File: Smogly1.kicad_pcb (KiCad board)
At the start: 2 copper layers, 92.2 x 68 mm, 9 parts, among them J1 VCC IN, J10 ESP32-DevKit VIN-EN, J11 ESP32-DevKit 3V3-D23, J2 PMSx003, J3 BME280, J4 microUSB, J5 5/3.3/GND, J8 D33/32/35/35, J9 PMS7003_Conn

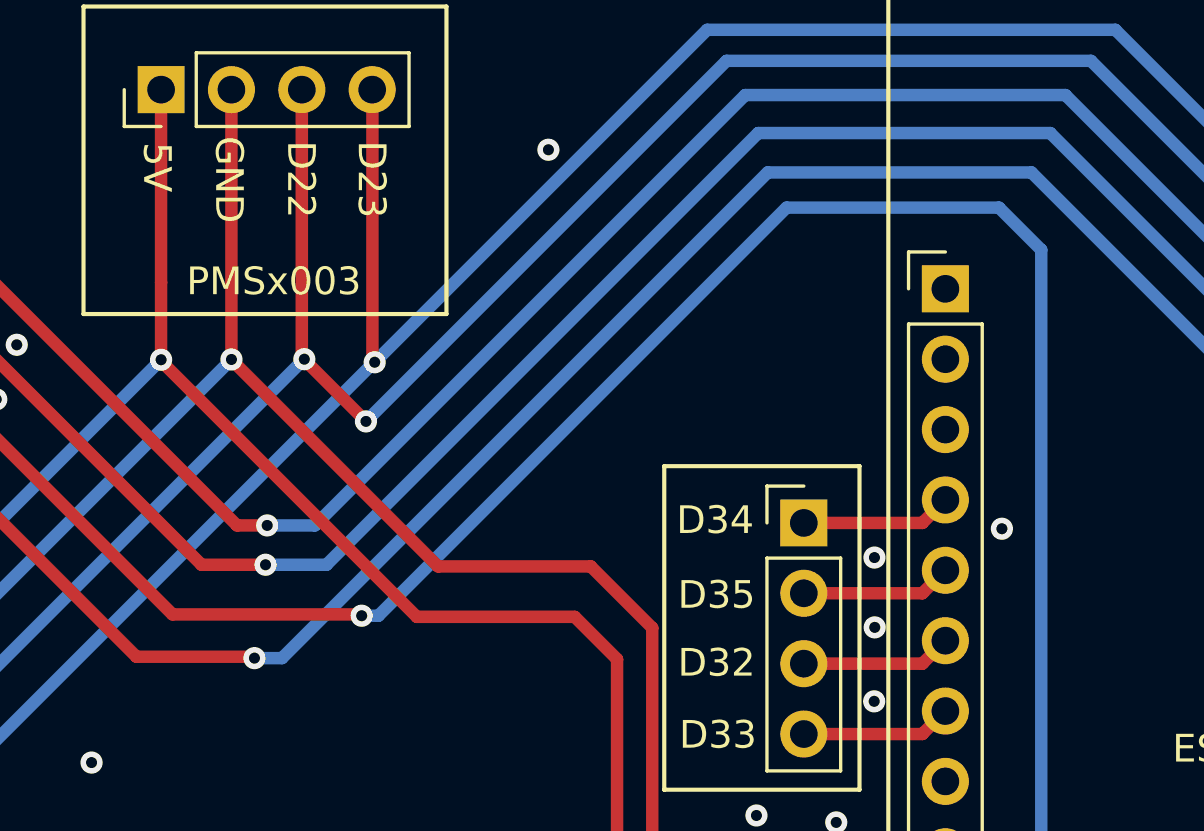
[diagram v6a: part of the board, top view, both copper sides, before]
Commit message: fixed wrong BME280 power connection (switch +3/G pins)
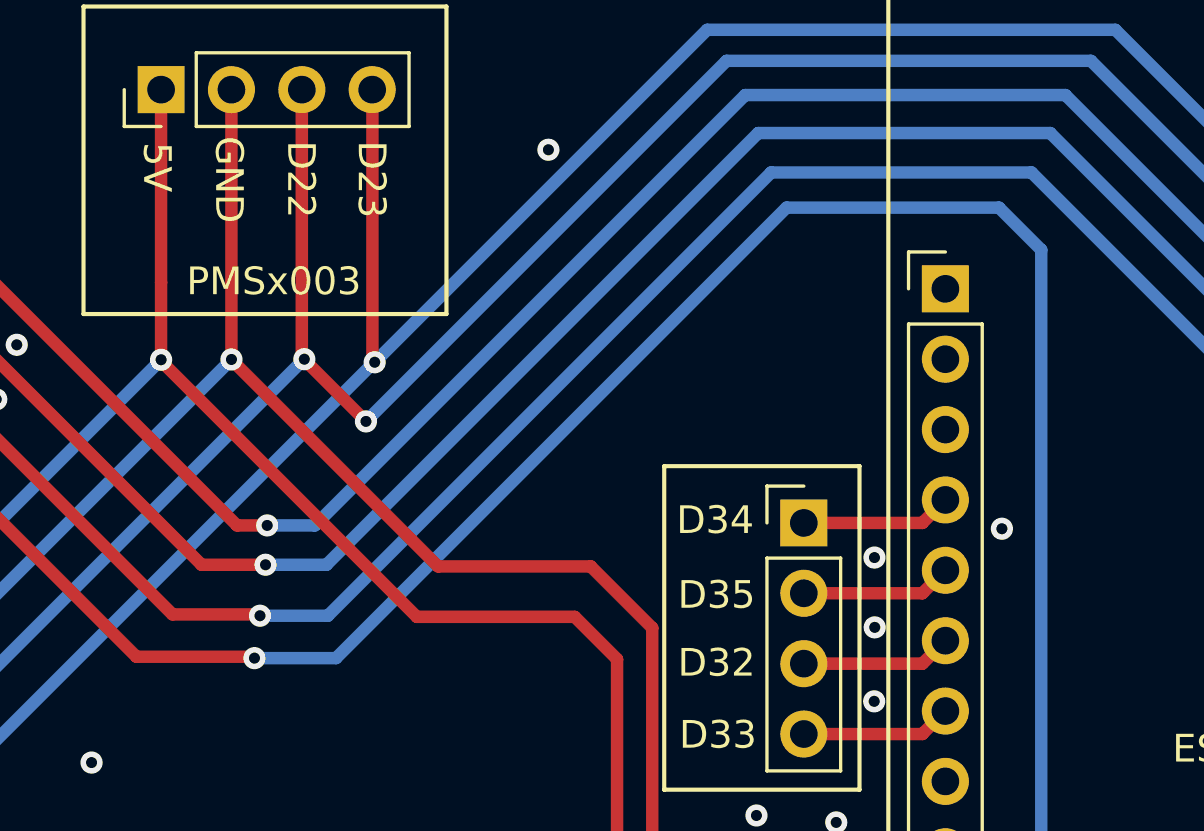
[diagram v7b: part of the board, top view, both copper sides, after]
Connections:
- J3 pad 3: +3V3 -> Net-(J11-Pad14)
- J3 pad 4: Net-(J11-Pad14) -> +3V3
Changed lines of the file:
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@@
       (net 13 "Net-(J11-Pad7)") (pinfunction "Pin_2") (pintype "passive"))
     (pad "3" thru_hole oval locked (at 0 5.08) (size 1.7 1.7) (drill 1) (layers *.Cu *.Mask)
-      (net 5 "+3V3") (pinfunction "Pin_3") (pintype "passive"))
+      (net 2 "Net-(J11-Pad14)") (pinfunction "Pin_3") (pintype "passive"))
     (pad "4" thru_hole oval locked (at 0 7.62) (size 1.7 1.7) (drill 1) (layers *.Cu *.Mask)
-      (net 2 "Net-(J11-Pad14)") (pinfunction "Pin_4") (pintype "passive"))
+      (net 5 "+3V3") (pinfunction "Pin_4") (pintype "passive"))
     (model "${KISYS3DMOD}/Connector_PinHeader_2.54mm.3dshapes/PinHeader_1x04_P2.54mm_Vertical.wrl"
       (offset (xyz 0 0 0))
@@
   (segment (start 250.39 82.65) (end 250.5 82.54) (width 0.45) (layer "B.Cu") (net 1))
   (segment (start 177.68 109.85) (end 177.68 107.02) (width 0.45) (layer "B.Cu") (net 1))
-  (segment (start 188.15 85.32) (end 185 85.32) (width 0.45) (layer "F.Cu") (net 2))
-  (segment (start 200.37 93.33) (end 200.32 93.28) (width 0.45) (layer "F.Cu") (net 2))
-  (segment (start 200.32 93.28) (end 196.11 93.28) (width 0.45) (layer "F.Cu") (net 2))
-  (segment (start 196.11 93.28) (end 188.15 85.32) (width 0.45) (layer "F.Cu") (net 2))
-  (via (at 200.37 93.33) (size 0.8) (drill 0.4) (layers "F.Cu" "B.Cu") (net 2))
-  (segment (start 218.8958 75.7992) (end 228.4192 75.7992) (width 0.45) (layer "B.Cu") (net 2))
+  (segment (start 188.44 82.78) (end 185 82.78) (width 0.45) (layer "F.Cu") (net 2))
+  (segment (start 197.41 91.75) (end 188.44 82.78) (width 0.45) (layer "F.Cu") (net 2))
+  (segment (start 200.52 91.75) (end 197.41 91.75) (width 0.45) (layer "F.Cu") (net 2))
+  (segment (start 200.57 91.8) (end 200.52 91.75) (width 0.45) (layer "F.Cu") (net 2))
+  (via (at 200.57 91.8) (size 0.8) (drill 0.4) (layers "F.Cu" "B.Cu") (net 2))
   (segment (start 246.37 108.89) (end 250.5 113.02) (width 0.45) (layer "B.Cu") (net 2))
-  (segment (start 201.365 93.33) (end 218.8958 75.7992) (width 0.45) (layer "B.Cu") (net 2))
+  (segment (start 203.02 91.8) (end 219.0208 75.7992) (width 0.45) (layer "B.Cu") (net 2))
+  (segment (start 246.37 93.75) (end 246.37 108.89) (width 0.45) (layer "B.Cu") (net 2))
+  (segment (start 200.57 91.8) (end 203.02 91.8) (width 0.45) (layer "B.Cu") (net 2))
   (segment (start 228.4192 75.7992) (end 246.37 93.75) (width 0.45) (layer "B.Cu") (net 2))
-  (segment (start 246.37 93.75) (end 246.37 108.89) (width 0.45) (layer "B.Cu") (net 2))
-  (segment (start 200.37 93.33) (end 201.365 93.33) (width 0.45) (layer "B.Cu") (net 2))
+  (segment (start 219.0208 75.7992) (end 228.4192 75.7992) (width 0.45) (layer "B.Cu") (net 2))
   (segment (start 224.76 116.11) (end 225.31 115.56) (width 0.45) (layer "F.Cu") (net 3))
   (segment (start 213.46 131.36) (end 215.225 133.125) (width 0.45) (layer "F.Cu") (net 3))
@@
   (segment (start 222 128.5) (end 224.05 130.55) (width 0.45) (layer "B.Cu") (net 4))
   (segment (start 175.91 106.18) (end 199.54 82.55) (width 0.45) (layer "B.Cu") (net 4))
-  (segment (start 204.19 91.75) (end 197.41 91.75) (width 0.45) (layer "F.Cu") (net 5))
   (segment (start 226.8004 117.8) (end 219.1 117.8) (width 0.45) (layer "F.Cu") (net 5))
-  (segment (start 188.44 82.78) (end 185 82.78) (width 0.45) (layer "F.Cu") (net 5))
+  (segment (start 188.15 85.32) (end 185 85.32) (width 0.45) (layer "F.Cu") (net 5))
   (segment (start 216.56 117.8) (end 219.1 117.8) (width 0.45) (layer "F.Cu") (net 5))
   (segment (start 228.72 115.45) (end 228.63 115.6656) (width 0.45) (layer "F.Cu") (net 5))
-  (segment (start 204.24 91.8) (end 204.19 91.75) (width 0.45) (layer "F.Cu") (net 5))
   (segment (start 228.63 115.6656) (end 228.63 115.9704) (width 0.45) (layer "F.Cu") (net 5))
-  (segment (start 197.41 91.75) (end 188.44 82.78) (width 0.45) (layer "F.Cu") (net 5))
+  (segment (start 200.37 93.33) (end 200.32 93.28) (width 0.45) (layer "F.Cu") (net 5))
   (segment (start 228.63 115.9704) (end 226.8004 117.8) (width 0.45) (layer "F.Cu") (net 5))
-  (via (at 204.24 91.8) (size 0.8) (drill 0.4) (layers "F.Cu" "B.Cu") (net 5))
+  (segment (start 200.32 93.28) (end 196.11 93.28) (width 0.45) (layer "F.Cu") (net 5))
+  (segment (start 196.11 93.28) (end 188.15 85.32) (width 0.45) (layer "F.Cu") (net 5))
+  (via (at 200.37 93.33) (size 0.8) (drill 0.4) (layers "F.Cu" "B.Cu") (net 5))
   (via (at 228.72 115.45) (size 0.8) (drill 0.4) (layers "F.Cu" "B.Cu") (net 5))
+  (segment (start 228.83 115.56) (end 250.5 115.56) (width 0.45) (layer "B.Cu") (net 5))
+  (segment (start 227.2468 77.0692) (end 219.5758 77.0692) (width 0.45) (layer "B.Cu") (net 5))
+  (segment (start 228.72 115.45) (end 228.7708 115.5248) (width 0.45) (layer "B.Cu") (net 5))
+  (segment (start 228.72 115.45) (end 228.83 115.56) (width 0.45) (layer "B.Cu") (net 5))
   (segment (start 228.7708 78.5932) (end 227.2468 77.0692) (width 0.45) (layer "B.Cu") (net 5))
-  (segment (start 228.72 115.45) (end 228.7708 115.5248) (width 0.45) (layer "B.Cu") (net 5))
-  (segment (start 219.5758 77.0692) (end 204.845 91.8) (width 0.45) (layer "B.Cu") (net 5))
-  (segment (start 228.83 115.56) (end 250.5 115.56) (width 0.45) (layer "B.Cu") (net 5))
-  (segment (start 204.845 91.8) (end 204.24 91.8) (width 0.45) (layer "B.Cu") (net 5))
-  (segment (start 228.72 115.45) (end 228.83 115.56) (width 0.45) (layer "B.Cu") (net 5))
-  (segment (start 227.2468 77.0692) (end 219.5758 77.0692) (width 0.45) (layer "B.Cu") (net 5))
   (segment (start 228.7708 115.5248) (end 228.7708 78.5932) (width 0.45) (layer "B.Cu") (net 5))
+  (segment (start 203.315 93.33) (end 200.37 93.33) (width 0.45) (layer "B.Cu") (net 5))
+  (segment (start 219.5758 77.0692) (end 203.315 93.33) (width 0.45) (layer "B.Cu") (net 5))
   (segment (start 220.2 88.45) (end 224.48 88.45) (width 0.45) (layer "F.Cu") (net 9))
   (segment (start 224.48 88.45) (end 225.31 87.62) (width 0.45) (layer "F.Cu") (net 9))

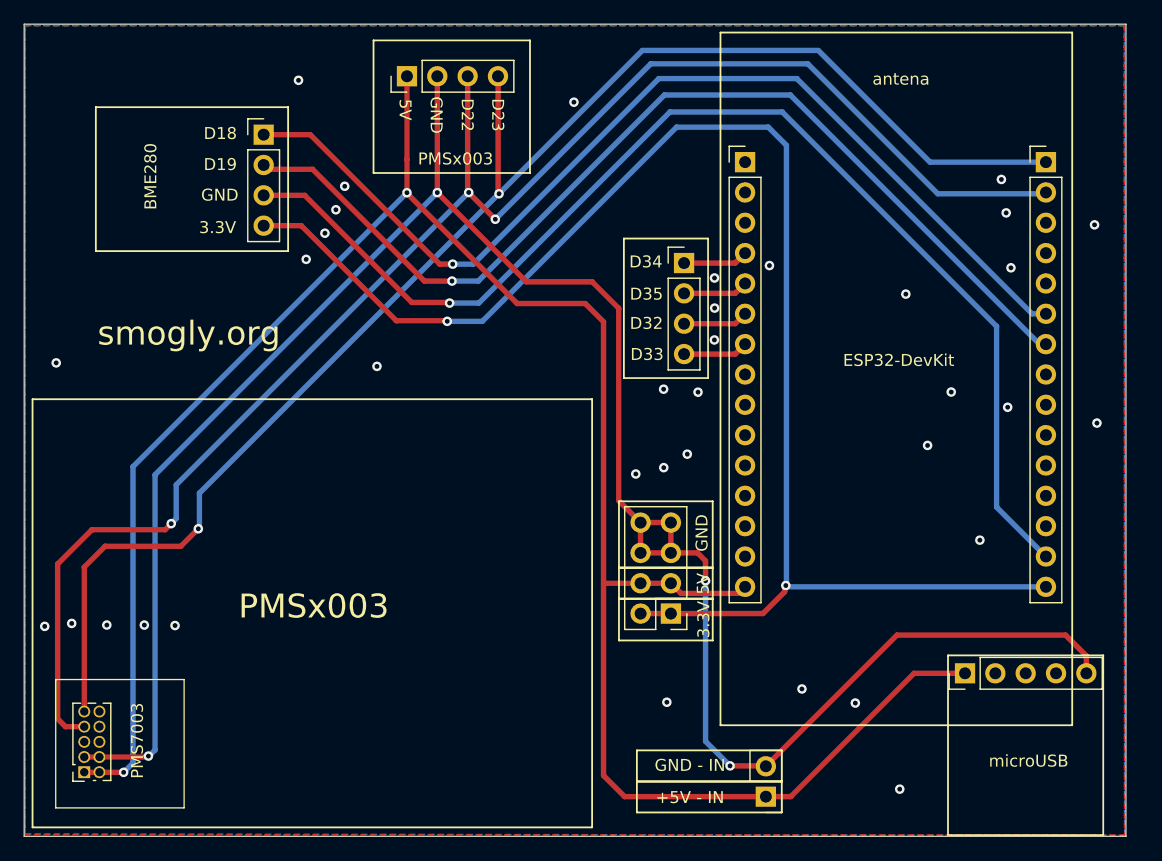
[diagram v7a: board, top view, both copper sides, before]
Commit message: Update to KiCad 7
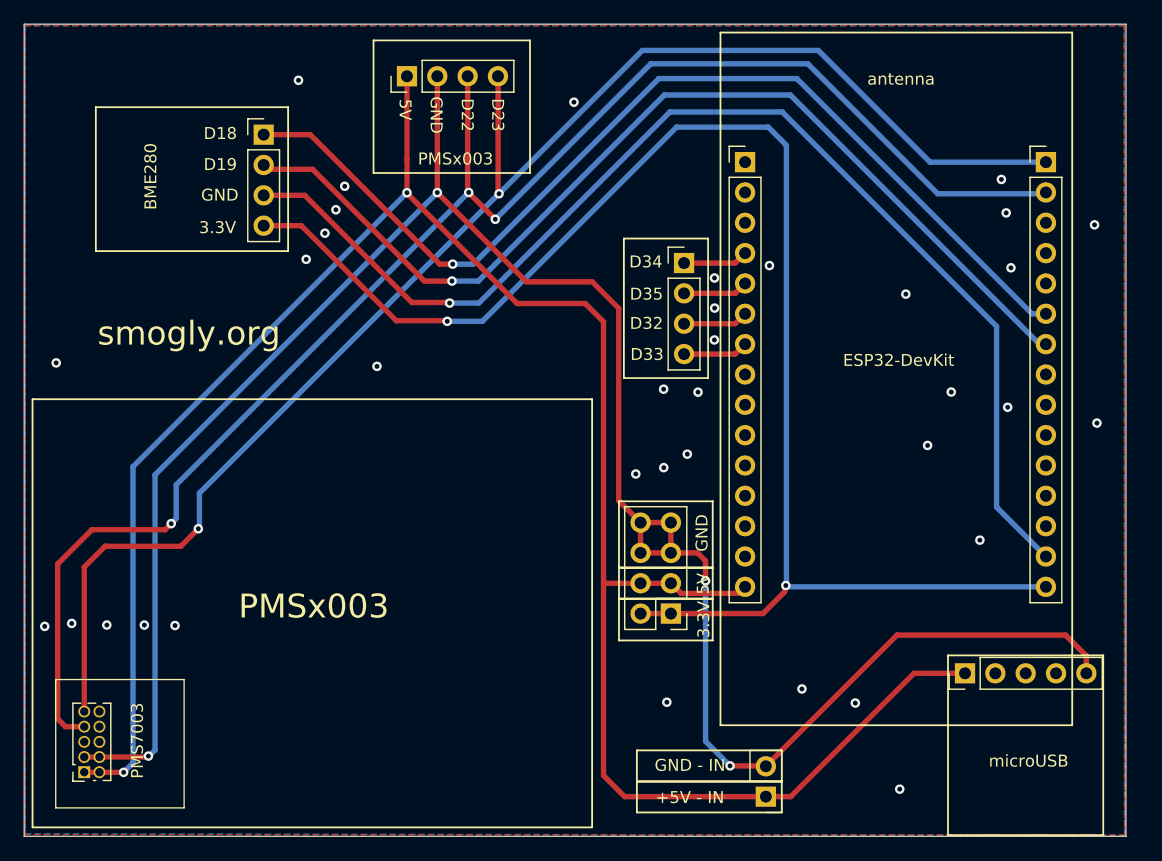
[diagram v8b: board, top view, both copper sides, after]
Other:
- board text added: "antenna"
- board text removed: "antena"
